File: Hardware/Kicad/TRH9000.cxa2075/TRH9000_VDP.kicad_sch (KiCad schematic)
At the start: 13 parts, among them U3 V9990, U4 KM428C256, U5 KM428C256, X1 14.31818MHz, Y1 21.47727Mhz

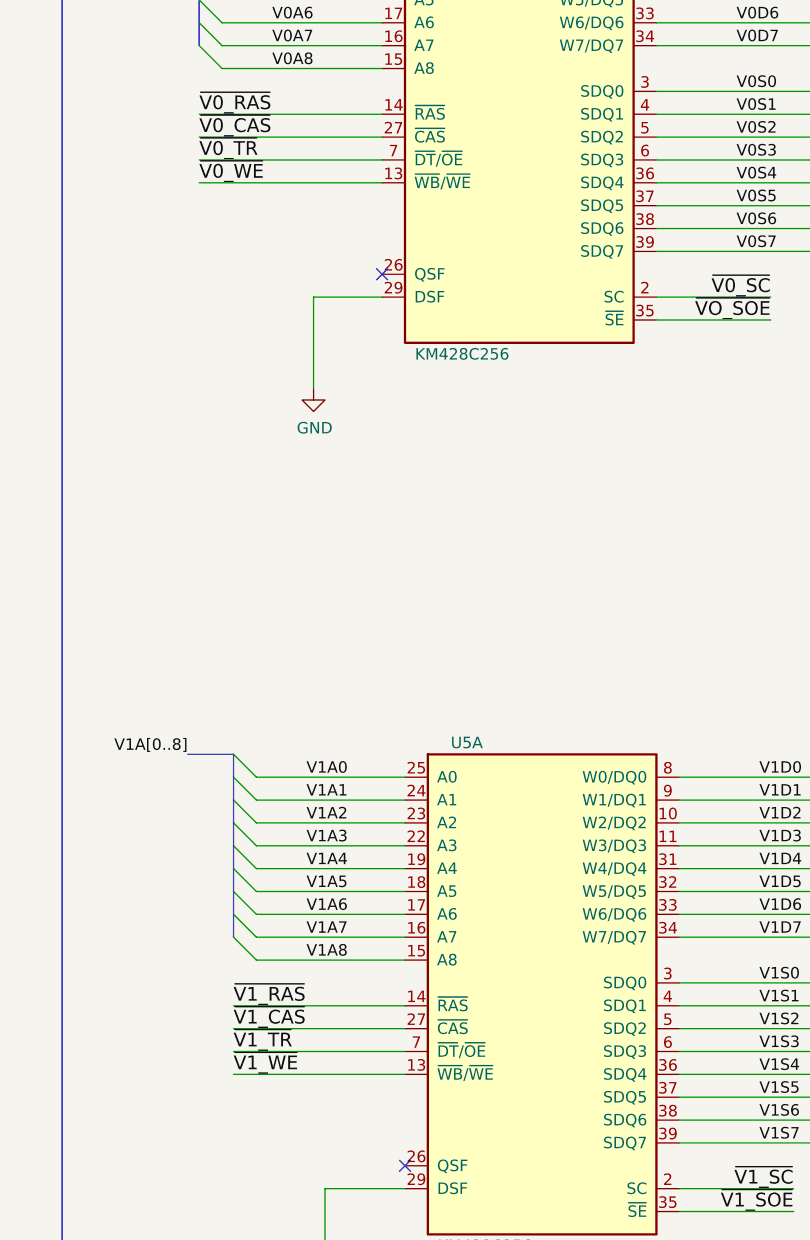
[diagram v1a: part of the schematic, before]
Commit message: Fix on VRAM wiring
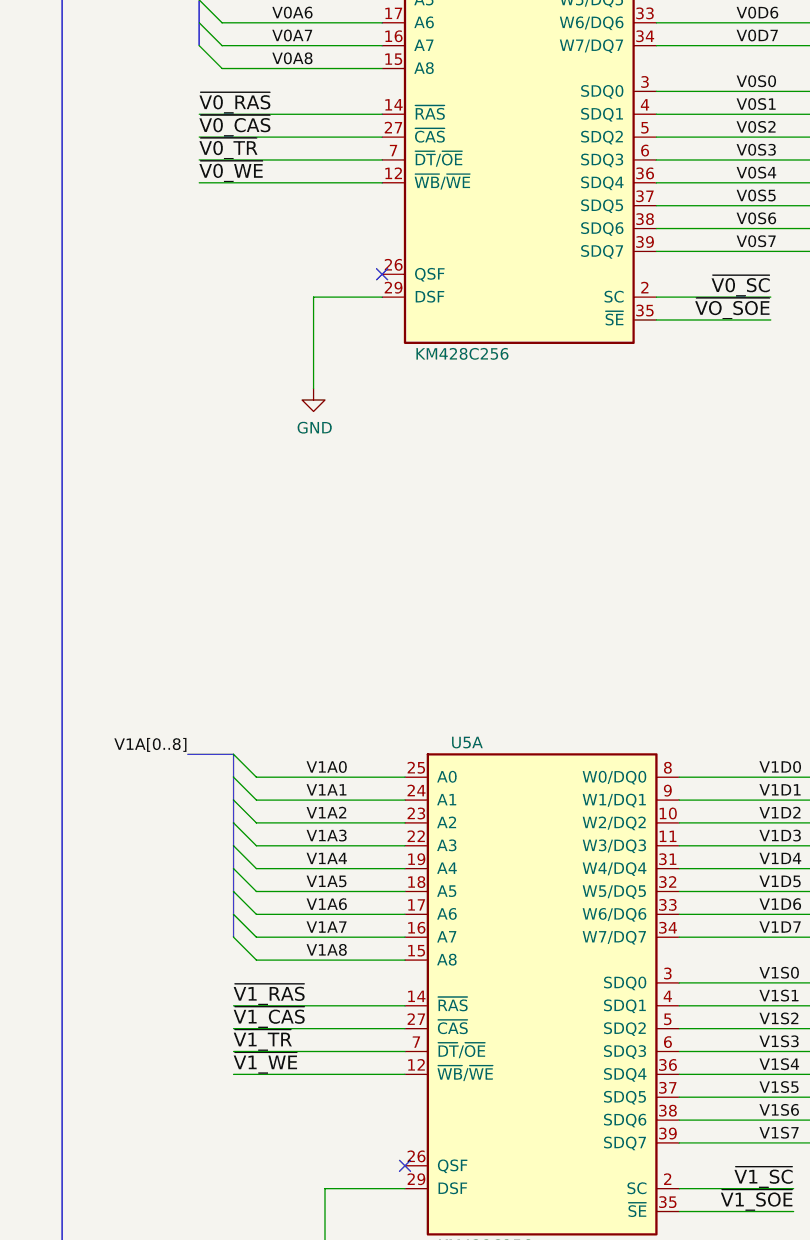
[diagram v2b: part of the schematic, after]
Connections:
- net ~{V0_WE}: now also U4.12 (~{WB}/~{WE}); no longer U4.13 (~{WB}/~{WE})
- net ~{V1_WE}: now also U5.12 (~{WB}/~{WE}); no longer U5.13 (~{WB}/~{WE})
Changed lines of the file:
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@@
   (title_block
     (title "TRH9000")
-    (date "2022-12-26")
-    (rev "1.2")
+    (date "2023-10-22")
+    (rev "1.3")
     (company "The Retro Hacker")
     (comment 2 "Shared under CERN-OHL-S license")
@@
     (pin "10")
     (pin "11")
-    (pin "13")
+    (pin "12")
     (pin "14")
     (pin "15")
@@
     (pin "9")
     (pin "1")
-    (pin "12")
+    (pin "13")
     (pin "20")
     (pin "21")
@@
     (pin "10")
     (pin "11")
-    (pin "13")
+    (pin "12")
     (pin "14")
     (pin "15")
@@
     (pin "9")
     (pin "1")
-    (pin "12")
+    (pin "13")
     (pin "20")
     (pin "21")

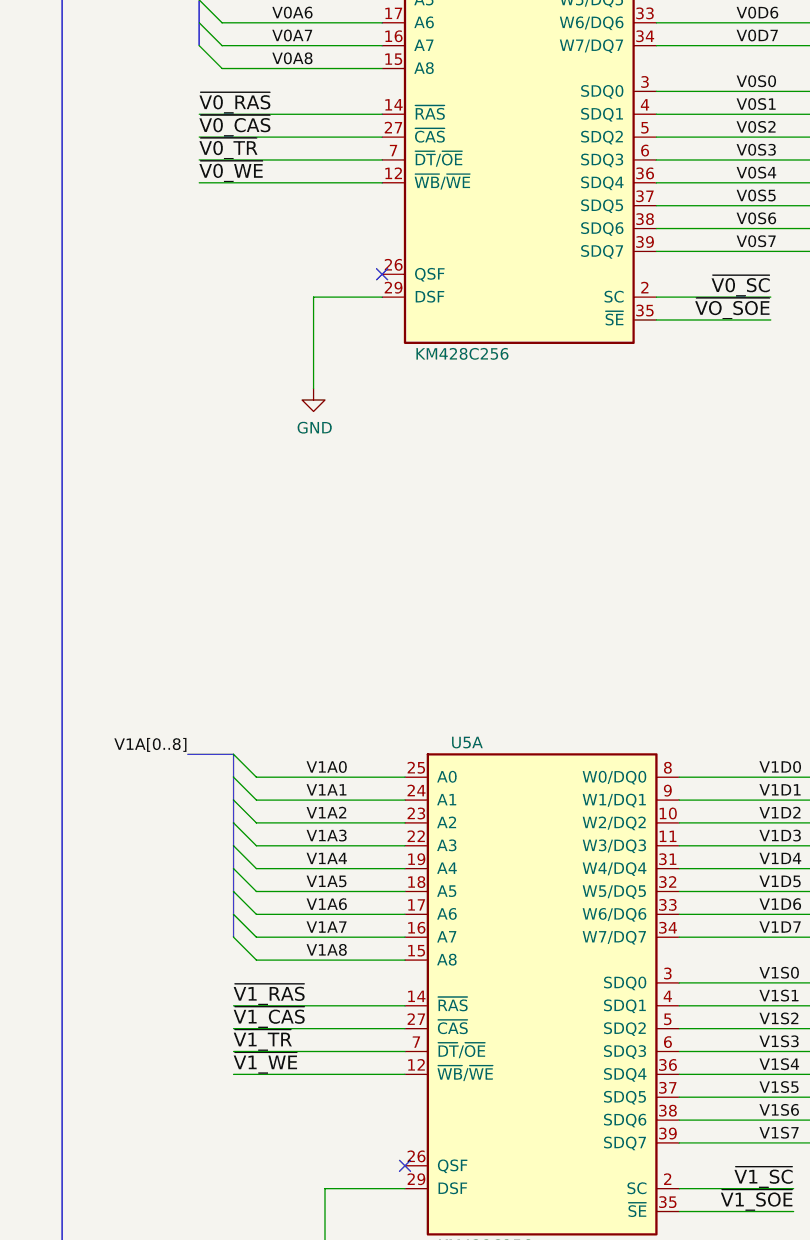
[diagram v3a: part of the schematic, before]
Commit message: Fix on pins 12 and 13 of the VRAM
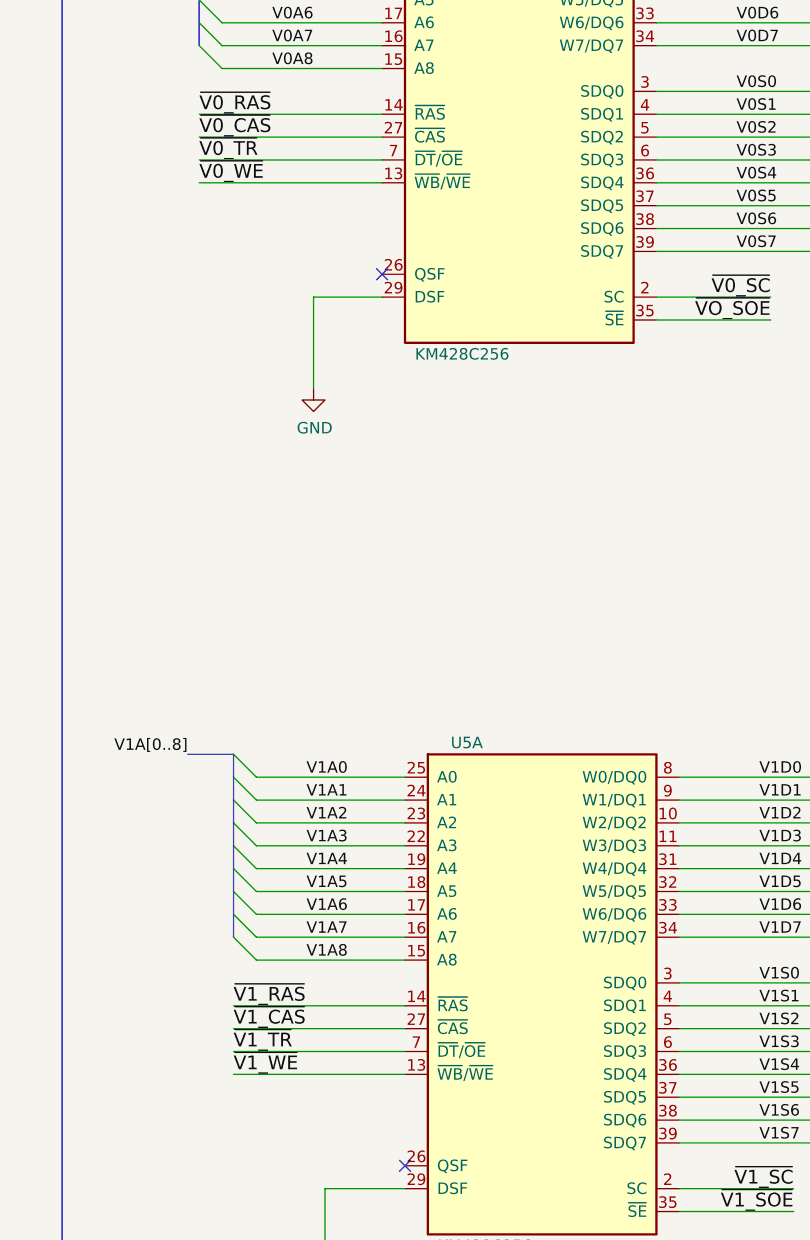
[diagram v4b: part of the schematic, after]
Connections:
- net ~{V0_WE}: now also U4.13 (~{WB}/~{WE}); no longer U4.12 (~{WB}/~{WE})
- net ~{V1_WE}: now also U5.13 (~{WB}/~{WE}); no longer U5.12 (~{WB}/~{WE})
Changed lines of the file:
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@@
     (pin "10")
     (pin "11")
-    (pin "12")
+    (pin "13")
     (pin "14")
     (pin "15")
@@
     (pin "9")
     (pin "1")
-    (pin "13")
+    (pin "12")
     (pin "20")
     (pin "21")
@@
     (pin "10")
     (pin "11")
-    (pin "12")
+    (pin "13")
     (pin "14")
     (pin "15")
@@
     (pin "9")
     (pin "1")
-    (pin "13")
+    (pin "12")
     (pin "20")
     (pin "21")

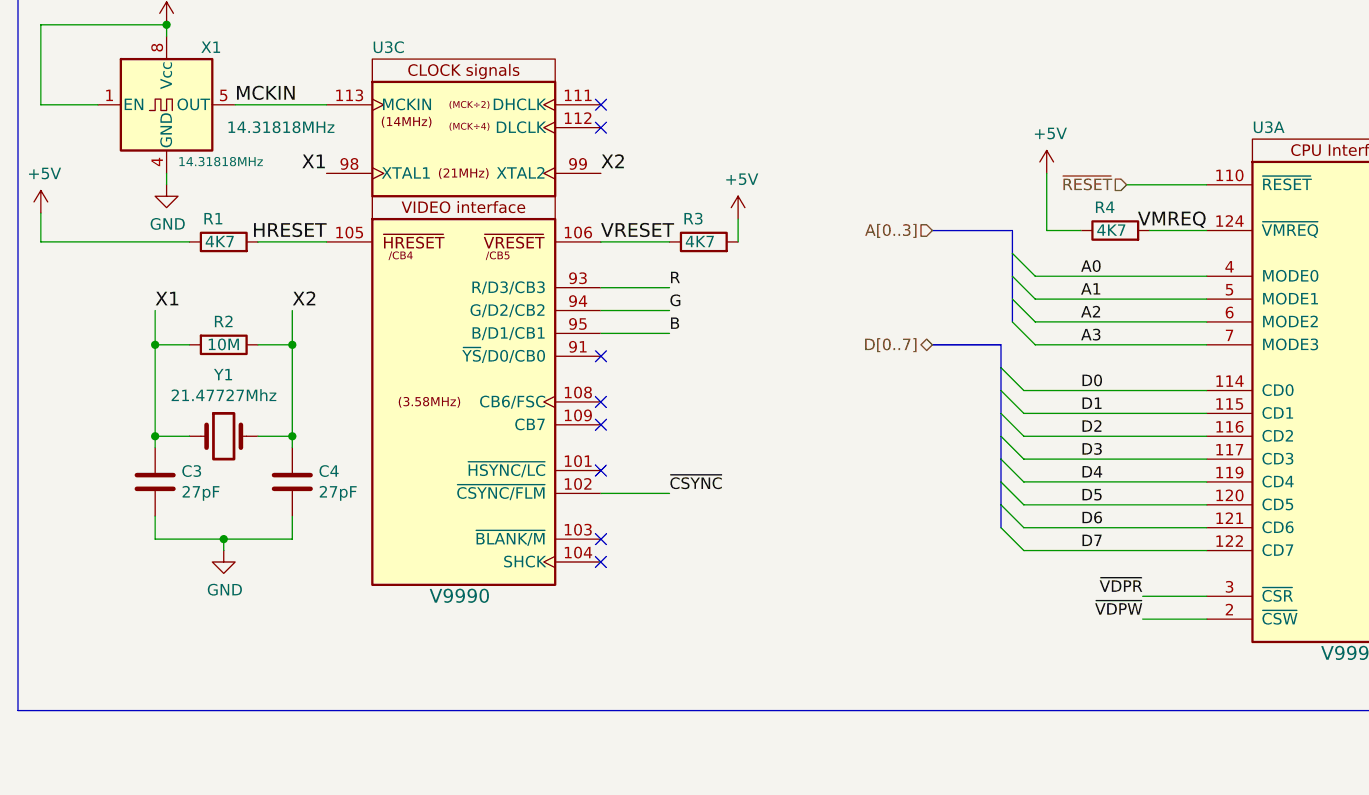
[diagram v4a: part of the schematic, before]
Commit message: kicad 8 migration. minor positioning for the connectors
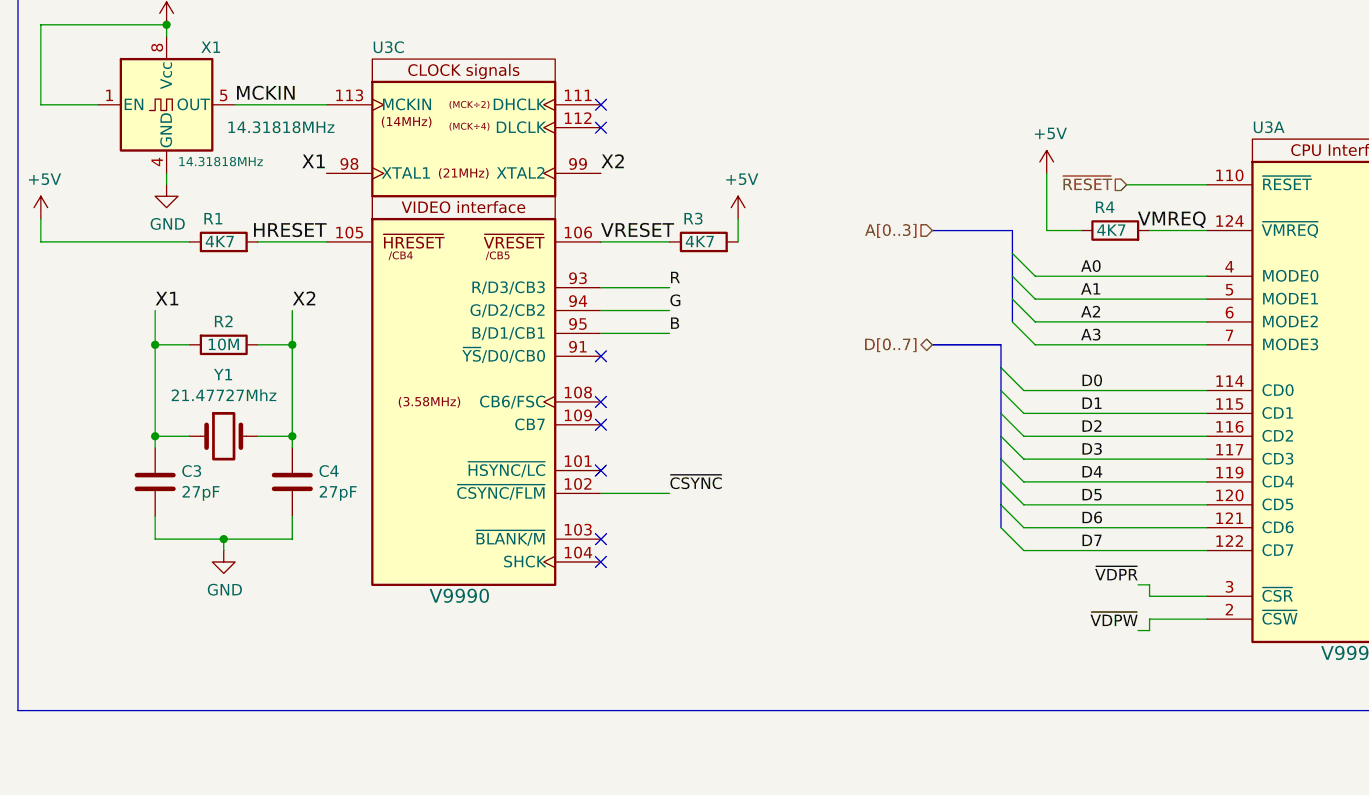
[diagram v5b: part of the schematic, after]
